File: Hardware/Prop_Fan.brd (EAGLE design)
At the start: 136 parts, among them J1 1546215-2, J2 1546215-2, J3 1546215-2, J4 1546215-2, SW2 EVQ-Q2203W, SW3 EVQ-Q2203W, SW4 EVQ-Q2203W, U1 P8X32A-Q44, U10 MAX31855KASA+, U11 MAX31855KASA+, U12 MF-DSC-SOT233-BSS138, U13 MF-DSC-SOT233-BSS138, U14 CD74HC595M96, U16 CD74HC165M96, U17 MF-DSC-SOT233-BSS138, U18 MF-DSC-SOT233-BSS138, U19 MF-DSC-SOT233-BSS138, U2 MF-DSC-SOT233-BSS138, U3 MF-DSC-SOT233-BSS138, U4 MAX31855KASA+, U5 LM22678TJ-5.0/NOPB, U6 ADP3338AKCZ-3.3-RL, U7 CAT24C512WI-GT3, U8 MF-DSC-SOT233-BSS138, U9 MAX31855KASA+, X1 ABMM-6.000MHZ-B2-T

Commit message: IMU E-compass added. Routing almost done.
Need to add a way to look at the dome brightness.
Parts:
- removed D4, D5, D6: MF-LED-0805-RED, PP_LED:LED_0805
- removed R43: 27K, MF_Passives:R0603
- removed R44, R47, R48, R49, R50, R51, R52: 10K, MF_Passives:R0603
- removed RELAYS1: 1-282834-0, PP_Connectors:1-282834-0
- removed SW4: EVQ-Q2203W, PP_Electromechanical:EVQ-Q2203W
- added 3.3V_PWR: MF-LED-0805-RED, PP_LED:LED_0805
- added C13: C3225X7S2A475M200AB, PP_Passives:1210
- added C25, C26, C37, C40, C8: 0.1uF, PP_Passives:0805
- added C36: 4.7uF, PP_Passives:0805
- added SW1: MF-SW-TACT-4.2MM, MF_Switches:TACT4.2MM
- added SWITCHS: 1-282834-0, PP_Connectors:1-282834-0
- added SW_D, SW_S, SW_U: 1546215-2, PP_Connectors:1546215-2
- added U$31, U$32, U$33, U$34: (no value), PP_Connectors:MOUNT_HOLE_150MIL
- added U$35: (no value), PP_Aesthetics:DB_COPPER_MEDIUM
- added U15, U20, U21, U22, U23, U24, U25, U26: G3VM-61GR2(TR05), PP_DigitalIC:G3VM-61GR2
- added U27: FXOS8700CQR1, PP_Sensors:FXOS8700CQR1
- BOARD_PWR: value (none) -> 1546215-2; device PP_Connectors:640454-3 -> PP_Connectors:1546215-2
- C17, C22, C6: device PP_Passives:0805 -> PP_Passives:1210
- C5, R11, R14, R18, R3, R4, R5, R6, R7, R8: device PP_Passives:0805 -> PP_Passives:0603
- R12: value 390 -> 10K; device PP_Passives:0805 -> PP_Passives:0603
- R13: value 1K -> 10K; device PP_Passives:0805 -> PP_Passives:0603
- R2: value 10K -> 470K; device PP_Passives:0805 -> PP_Passives:0603
- R27, R37, R39, R41: value 27K -> 1.2K
- R31, R33, R35: value 27K -> 10K
- R36, R38, R40, R42: value 10K -> 1.2K
- SW2, SW3: value EVQ-Q2203W -> MF-SW-TACT-4.2MM; device PP_Electromechanical:EVQ-Q2203W -> MF_Switches:TACT4.2MM
- U12, U13, U17, U18, U19, U2, U3, U8: value MF-DSC-SOT233-BSS138 -> G3VM-61GR2(TR05); device MF_Discrete_Semiconductor:SOT-23-3 -> PP_DigitalIC:G3VM-61GR2
- moved R37 765.7 mm to (134.4, 61.2), turned to 90 degrees
- moved R39 765.4 mm to (129.3, 61.2), turned to 90 degrees
- moved R41 765.1 mm to (124.2, 61.2), turned to 90 degrees
- moved R36 764.5 mm to (136.9, 61.2), turned to 90 degrees
- moved R38 762.0 mm to (131.8, 61.2), turned to 90 degrees
- moved R40 761.7 mm to (126.7, 61.2), turned to 90 degrees
- moved R42 761.5 mm to (121.7, 61.2), turned to 90 degrees
- moved R27 746.9 mm to (139.4, 61.2), turned to 90 degrees
- moved R35 735.7 mm to (120.6, 41.0), turned to 270 degrees
- moved R34 735.2 mm to (124.1, 41.0), turned to 270 degrees
- moved R33 733.5 mm to (125.7, 41.0), turned to 270 degrees
- moved R28 733.4 mm to (138.4, 41.0), turned to 270 degrees
- moved R32 732.8 mm to (129.0, 41.0), turned to 270 degrees
- moved R31 731.2 mm to (130.7, 41.0), turned to 270 degrees
- moved U19 717.8 mm to (138.2, 55.1), turned to 180 degrees
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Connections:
- net OUT_OPTO_0 renamed OUT_0
- net OUT_OPTO_1 renamed OUT_1
- net OUT_OPTO_2 renamed OUT_2
- net OUT_OPTO_3 renamed OUT_3
- net OUT_OPTO_4 renamed OUT_4
- net OUT_OPTO_5 renamed OUT_5
- net OUT_OPTO_6 renamed OUT_6
- net OUT_OPTO_7 renamed OUT_7
- removed net P$1: R29.P$1, R30.P$1, R47.P$1, R48.P$1, R49.P$1, R50.P$1, R51.P$1, R52.P$1, U12.P$2, U13.P$2, U17.P$2, U18.P$2, U19.P$2, U2.P$2, U3.P$2, U8.P$2
- removed net P19: U1.22
- removed net P20: U1.23
- removed net P21: U1.24
- new net N$1: R28.P$1, U16.11, U19.P$4
- new net N$10: R38.P$1, U22.P$1
- new net N$19: R39.P$1, U23.P$1
- new net N$20: R40.P$1, U24.P$1
- new net N$21: R41.P$1, U25.P$1
- new net N$22: R42.P$1, U26.P$1
- new net N$23: R27.P$2, SWITCHS.P$1
- new net N$24: R36.P$2, SWITCHS.P$2
- new net N$25: R37.P$2, SWITCHS.P$3
- new net N$26: R38.P$2, SWITCHS.P$4
- new net N$27: R39.P$2, SWITCHS.P$5
- new net N$28: R40.P$2, SWITCHS.P$6
- new net N$29: R41.P$2, SWITCHS.P$7
- new net N$3: R27.P$1, U19.P$1
- new net N$30: R42.P$2, SWITCHS.P$8
- new net N$31: R2.2, U5.P$7
- new net N$4: R36.P$1, U20.P$1
- new net N$6: R37.P$1, U21.P$1
- new net P0: U1.41
- new net SCL_1: R12.1, U1.11, U27.P$4
- new net SDA_1: R13.1, U1.10, U27.P$6
- new net T+_3: C12.1, D10.1, J4.P$1, U4.3
- new net T-_3: C12.2, D10.2, J4.P$2, U4.2
- net 12V_CLEAN: now also R2.1; no longer R13.2
- net 165_CLK: now also U1.14; no longer U1.15
- net 165_DATA: now also U1.12; no longer U1.16
- net 165_LOAD: now also U1.13; no longer U1.19
- net 3.3V: now also C25.1, C36.1, C37.1, C8.1, R12.2, R13.2, R28.P$2, R29.P$2, R30.P$2, R31.P$2, R32.P$2, R33.P$2, R34.P$2, R35.P$2, U27.P$1, U27.P$14; no longer R2.2
- net 595_CLK: now also U1.19; no longer U1.12
- net 595_DATA: now also U1.15; no longer U1.13
- net 595_LAT: now also U1.16; no longer U1.14
- net 5V_PWR: now also C13.1; no longer R12.2
- net CHASSIS_GND: now also BOARD_PWR.P$2, U12.P$3, U13.P$3, U15.P$3, U17.P$3, U18.P$3, U19.P$2, U2.P$3, U20.P$2, U21.P$2, U22.P$2, U23.P$2, U24.P$2, U25.P$2, U26.P$2, U3.P$3, U8.P$3; no longer BOARD_PWR.P$3
- net GND: now also 3.3V_PWR.CATHODE, C13.2, C25.2, C26.2, C36.2, C37.2, C40.2, C8.2, SW1.P$4, SW2.P$4, SW3.P$4, SW_D.P$2, SW_S.P$2, SW_U.P$2, U12.P$2, U13.P$2, U15.P$2, U17.P$2, U18.P$2, U19.P$3, U2.P$2, U20.P$3, U21.P$3, U22.P$3, U23.P$3, U24.P$3, U25.P$3, U26.P$3, U27.P$10, U27.P$12, U27.P$13, U27.P$16, U27.P$3, U27.P$5, U27.P$7, U3.P$2, U8.P$2; no longer D4.CATHODE, D5.CATHODE, D6.CATHODE, SW2.3, SW2.4, SW3.3, SW3.4, SW4.3, SW4.4
- net IN_OPTO_1: now also R29.P$1, U20.P$4; no longer R27.P$1, R28.P$1
- net IN_OPTO_2: now also R30.P$1, U21.P$4
- net IN_OPTO_3: now also R31.P$1, U22.P$4
- net IN_OPTO_4: now also R32.P$1, U23.P$4
- net IN_OPTO_5: now also R33.P$1, U24.P$4
- net IN_OPTO_6: now also R34.P$1, U25.P$4
- net IN_OPTO_7: now also R35.P$1, U26.P$4
- net N$11: no longer R29.P$2
- net N$12: no longer R30.P$2
- net N$13: no longer R47.P$2
- net N$14: no longer R48.P$2
- net N$15: no longer R49.P$2
- net N$16: now also U15.P$1; no longer R50.P$2, U17.P$1
- net N$17: now also U17.P$1; no longer R51.P$2, U18.P$1
- net N$18: now also U18.P$1; no longer R52.P$2, U19.P$1
- net N$7: now also C26.1, U27.P$2; no longer D6.ANODE, R13.1
- net N$8: now also C40.1, U27.P$8; no longer D5.ANODE, R12.1
- net N$9: now also 3.3V_PWR.ANODE; no longer D4.ANODE
- net PROP_D4: now also U1.44; no longer U1.4
- net PROP_D5: now also U1.1; no longer U1.9
- net PROP_D6: now also U1.42; no longer U1.10
- net PROP_D7: now also U1.43; no longer U1.11
- net PROP_E2: now also U1.9; no longer U1.3
- net PROP_R/W: now also U1.3; no longer U1.1
- net PROP_RES: no longer R2.1
- net PROP_RS: now also U1.4; no longer U1.44
- net RLY_0: now also U2.P$4; no longer U2.P$3
- net RLY_1: now also U3.P$4; no longer U3.P$3
- net RLY_2: now also U8.P$4; no longer U8.P$3
- net RLY_3: now also U12.P$4; no longer U12.P$3
- net RLY_4: now also U13.P$4; no longer U13.P$3
- net RLY_5: now also U15.P$4; no longer U17.P$3
- net RLY_6: now also U17.P$4; no longer U18.P$3
- net RLY_7: now also U18.P$4; no longer U19.P$3
- net SW_D: now also SW3.P$1, SW_D.P$1, U1.22; no longer SW4.1, SW4.2, U1.43
- net SW_S: now also SW2.P$1, SW_S.P$1, U1.23; no longer SW3.1, SW3.2, U1.42
- net SW_U: now also SW1.P$1, SW_U.P$1, U1.24; no longer SW2.1, SW2.2, U1.41
- net T+_0: now also D8.1; no longer D8.2
- net T+_1: now also D9.1; no longer C39.1, D7.2, D9.2, J3.P$1, U11.3
- net T+_2: now also C39.1, D7.1, J3.P$1, U11.3; no longer C12.1, D10.2, J4.P$1, U4.3
- net T-_0: now also D8.2; no longer D8.1
- net T-_1: now also D9.2; no longer C39.2, D7.1, D9.1, J3.P$2, U11.2
- net T-_2: now also C39.2, D7.2, J3.P$2, U11.2; no longer C12.2, D10.1, J4.P$2, U4.2
- net TC_SCK: now also U1.34; no longer U1.33
- net TC_SO: now also U1.33; no longer U1.34
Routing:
- net 3.3V: track 0.00 -> 279.4 mm, vias 0 -> 26
- net GND: track 22.6 -> 181.3 mm, vias 0 -> 135
- net PROP_E2: track 0.00 -> 97.4 mm
- net PROP_RS: track 0.00 -> 86.8 mm
- net PROP_R/W: track 0.00 -> 83.8 mm
- net PROP_E1: track 0.00 -> 81.0 mm
- net PROP_D5: track 0.00 -> 77.8 mm
- net PROP_D4: track 0.00 -> 74.3 mm
- net PROP_D7: track 0.00 -> 73.0 mm
- net PROP_D6: track 0.00 -> 71.7 mm
- net CHASSIS_GND: track 56.6 -> 118.7 mm, vias 0 -> 16
- net TC_SCK: track 0.00 -> 61.8 mm, vias 0 -> 5
- net SDA_1: track 0.00 -> 59.9 mm
- net SCL_1: track 0.00 -> 59.1 mm
- net TC_CS_1: track 0.00 -> 55.3 mm
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- added copper zone on layer 1, net 12V_BATT
- added copper zone on layer 1, net 12V_BATT_ON
- added copper zone on layer 1, net 12V_CLEAN
- added copper zone on layer 1, net 3.3V
- added copper zone on layer 16, net 3.3V
- added copper zone on layer 1, net 5V_PWR
- added copper zone on layer 1, net CHASSIS_GND
- added copper zone on layer 16, net CHASSIS_GND
- added copper zone on layer 1, net GND
- added copper zone on layer 16, net GND
- added copper zone on layer 1, net N$5
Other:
- board outline added: 152.9 x 71.1 mm

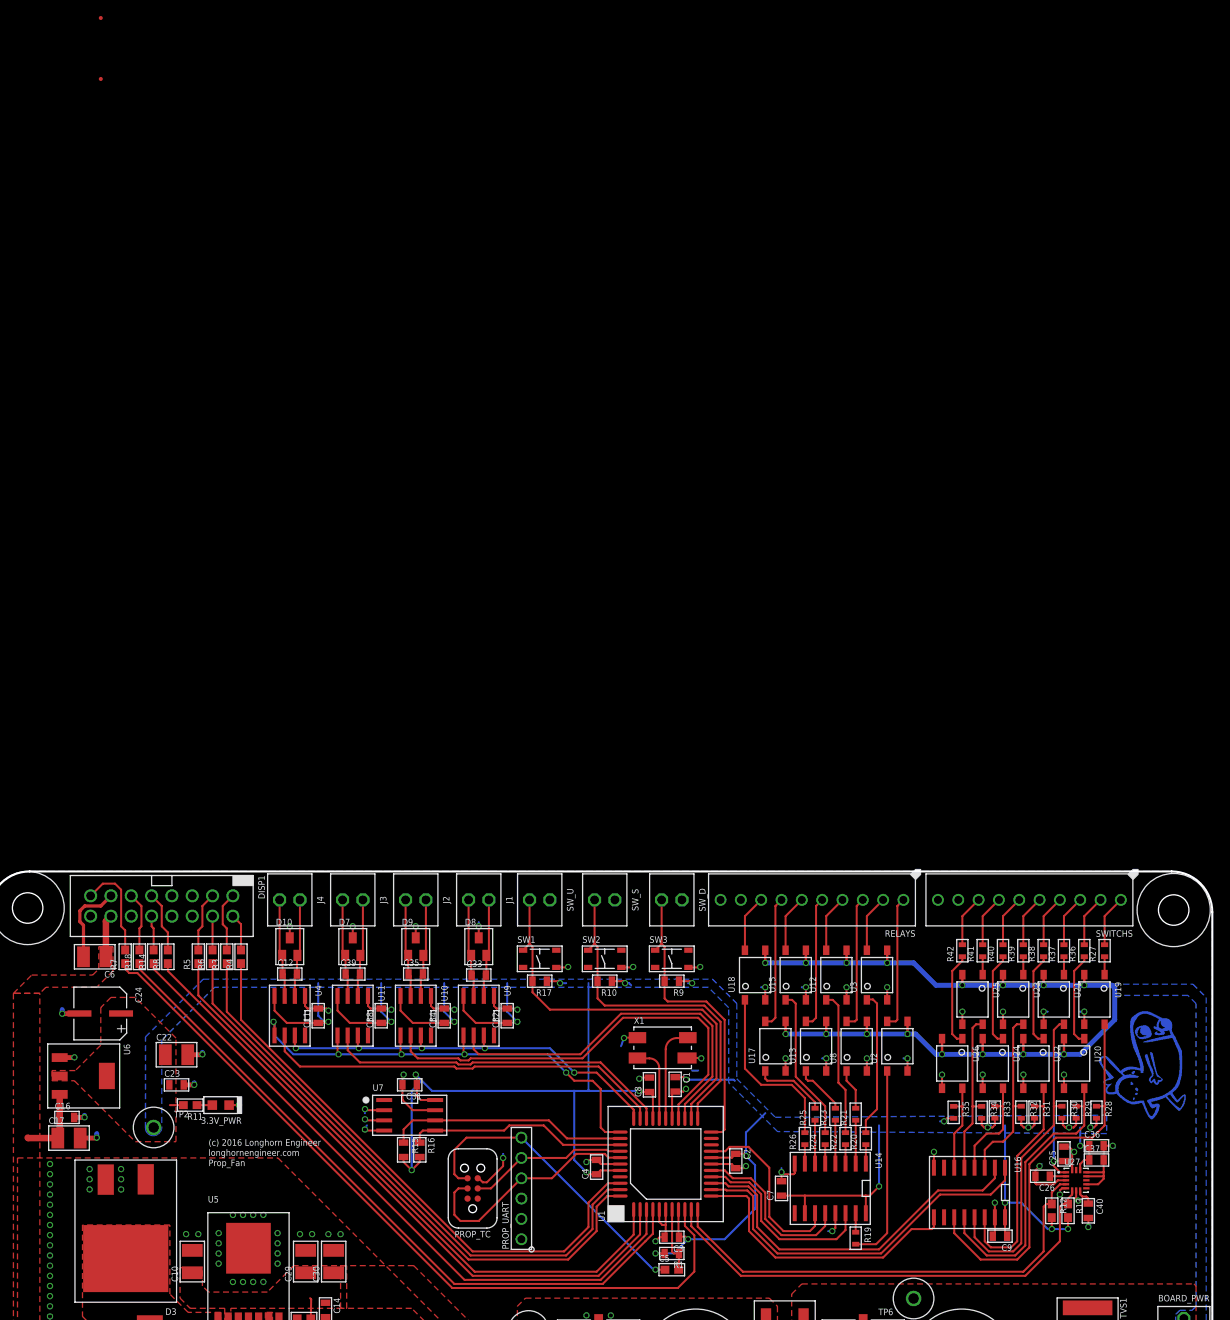
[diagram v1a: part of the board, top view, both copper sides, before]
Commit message: Corrected fids and added layout image.
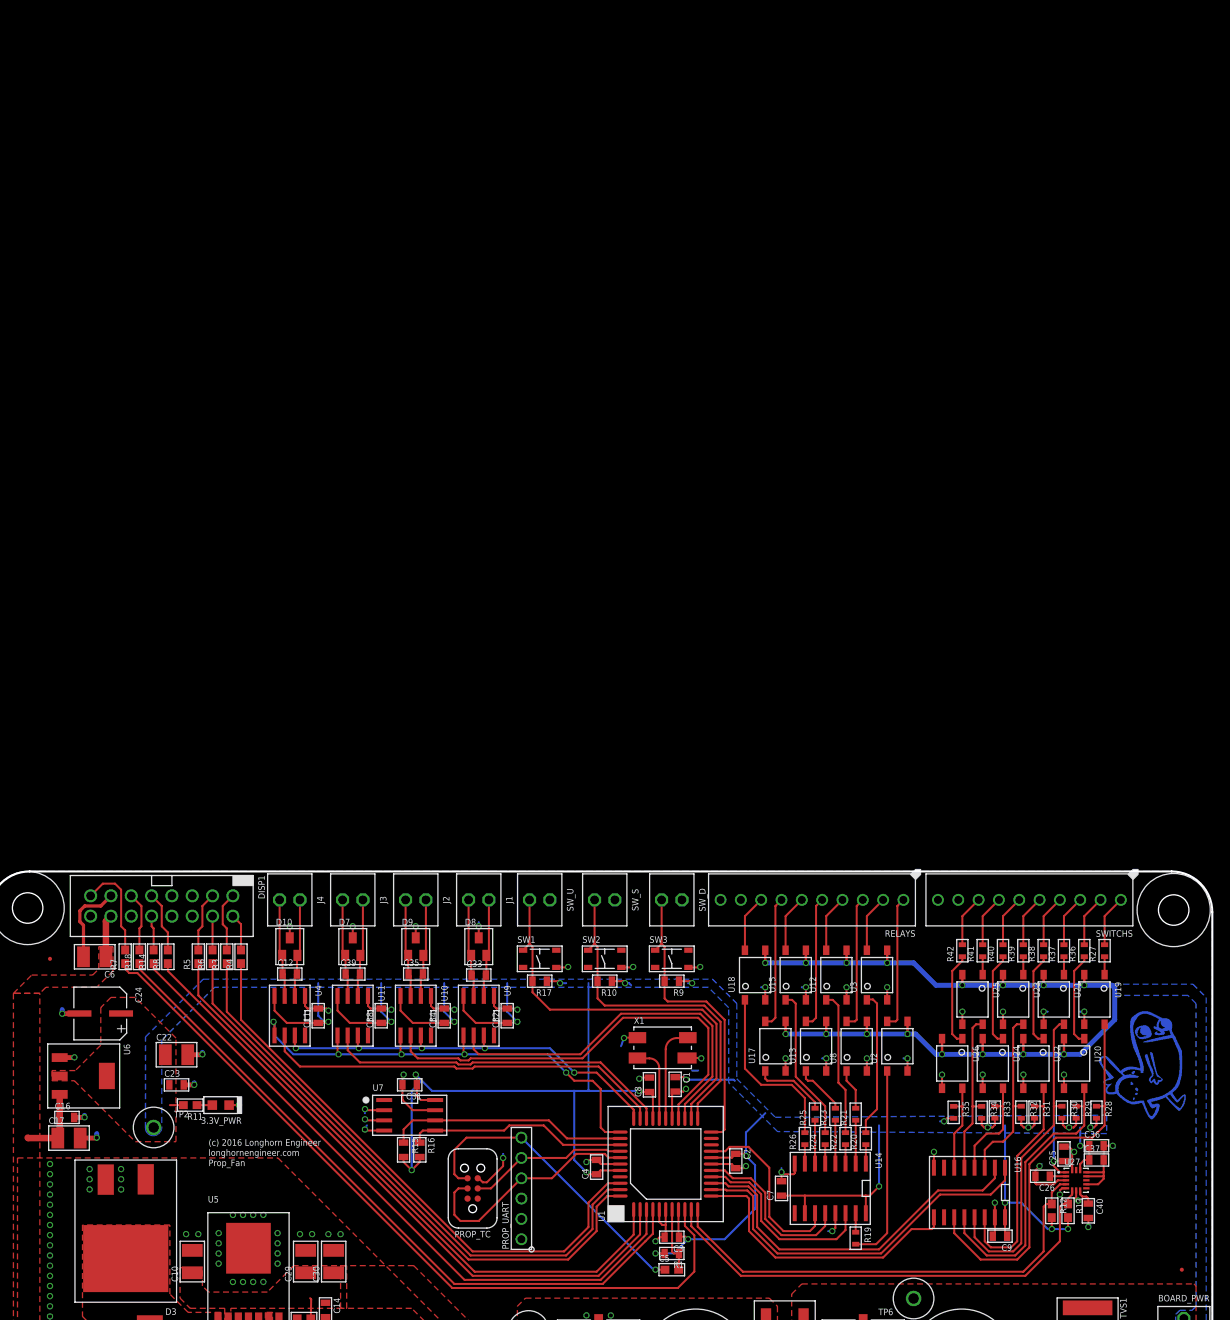
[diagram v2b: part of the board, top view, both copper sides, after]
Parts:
- moved FID2 201.0 mm to (149.1, 21.3)
- moved FID1 117.8 mm to (7.62, 60.2)
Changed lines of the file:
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@@
 <attribute name="REVNUM" value="REV: 1" x="27.432" y="31.75" size="1.778" layer="27" display="off"/>
 </element>
-<element name="FID1" library="MF_Aesthetics" package="FIDUCIAL_0.5MM" value="FIDUCIAL_0.5MM" x="13.97" y="177.8"/>
-<element name="FID2" library="MF_Aesthetics" package="FIDUCIAL_0.5MM" value="FIDUCIAL_0.5MM" x="13.97" y="170.18"/>
+<element name="FID1" library="MF_Aesthetics" package="FIDUCIAL_0.5MM" value="FIDUCIAL_0.5MM" x="7.62" y="60.198"/>
+<element name="FID2" library="MF_Aesthetics" package="FIDUCIAL_0.5MM" value="FIDUCIAL_0.5MM" x="149.098" y="21.336"/>
 <element name="X1" library="MF_Frequency_Control" package="7MMX5MM" value="ABMM-6.000MHZ-B2-T" x="84.201" y="49.0728"/>
 <element name="U1" library="MF_IC_Digital" package="LQFP44" value="P8X32A-Q44" x="84.582" y="34.544" rot="R90"/>

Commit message: PROP  Fan Rev 1 complete.
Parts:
- removed U$35: (no value), PP_Aesthetics:DB_COPPER_MEDIUM
- added C41, C42, C43: .1uF, PP_Passives:0603
- added C44, C45: 10uF, PP_Passives:1210
- added J5: 1546215-2, PP_Connectors:1546215-2
- added R43, R44, R45: 220, MF_Passives:R0603
- added U28: ACPL-C870-000E, PP_AnalogIC:ACPL-C87_SSO-8
- added U29: MAX11613EUA+, PP_AnalogIC:MAX11613_UMAX-8
- added U30: TPS7B6950QDBVRQ1, MF_IC_Power:SOT-23-5
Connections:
- new net A0: R43.P$2, U29.P$1
- new net A1: U29.P$2
- new net A2: U29.P$3
- new net A3: U29.P$4
- new net EXT_5V: C45.1, U28.P$1, U30.P$5
- new net N$32: C42.1, R43.P$1, U28.P$7
- new net N$33: R44.P$2, R45.P$2, U28.P$2
- new net N$36: J5.P$1, R45.P$1
- net 12V_BATT_ON: now also C44.1, U30.P$1
- net 3.3V: now also C41.1, C43.1, U28.P$8, U29.P$8
- net CHASSIS_GND: now also C44.2, C45.2, R44.P$1, U28.P$3, U28.P$4, U30.P$3, U30.P$4
- net GND: now also C41.2, C42.2, C43.2, U28.P$5, U28.P$6, U29.P$7
- net SCL_1: now also U29.P$5
- net SDA_1: now also U29.P$6
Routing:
- net 12V_BATT_ON: track 0.00 -> 55.7 mm, vias 0 -> 1
- net 3.3V: track 279.4 -> 313.3 mm, vias 26 -> 28
- net CHASSIS_GND: track 118.7 -> 151.9 mm, vias 16 -> 20
- net EXT_5V: track 0.00 -> 19.1 mm
- net GND: track 181.3 -> 197.2 mm, vias 135 -> 138
- net N$32: track 0.00 -> 15.3 mm
- net N$33: track 0.00 -> 7.51 mm
- net SCL_1: track 59.1 -> 65.8 mm, vias 0 -> 2
- net N$36: track 0.00 -> 4.08 mm
- net A0: track 0.00 -> 2.45 mm
- net SDA_1: track 59.9 -> 62.2 mm
